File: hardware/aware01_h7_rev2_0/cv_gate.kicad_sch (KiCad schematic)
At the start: 44 parts, among them J1 CV3_IN, J10 CV2_IN, J11 V/OCT_IN, J12 CV1_IN, J13 GATE3_IN, J14 GATE4_IN, J8 GATE1_IN, J9 GATE2_IN, Q1 MMBT3904, Q2 MMBT3904, Q3 MMBT3904, Q4 MMBT3904, U11 LMV722IDR, U12 LMV722IDR

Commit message: add 5V buck converter
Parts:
- J1, J10, J11, J12, J13, J14, J8, J9: footprint Connector_Audio:Jack_3.5mm_QingPu_WQP-PJ398SM_Vertical_CircularHoles -> AudioJacks:Jack_3.5mm_QingPu_WQP-PJ398SM_Vertical
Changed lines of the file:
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@@
 			)
 		)
-		(property "Footprint" "Connector_Audio:Jack_3.5mm_QingPu_WQP-PJ398SM_Vertical_CircularHoles"
+		(property "Footprint" "AudioJacks:Jack_3.5mm_QingPu_WQP-PJ398SM_Vertical"
 			(at 27.94 96.52 0)
 			(effects
@@
 			)
 		)
-		(property "Footprint" "Connector_Audio:Jack_3.5mm_QingPu_WQP-PJ398SM_Vertical_CircularHoles"
+		(property "Footprint" "AudioJacks:Jack_3.5mm_QingPu_WQP-PJ398SM_Vertical"
 			(at 27.94 55.88 0)
 			(effects
@@
 			)
 		)
-		(property "Footprint" "Connector_Audio:Jack_3.5mm_QingPu_WQP-PJ398SM_Vertical_CircularHoles"
+		(property "Footprint" "AudioJacks:Jack_3.5mm_QingPu_WQP-PJ398SM_Vertical"
 			(at 200.66 128.27 0)
 			(effects
@@
 			)
 		)
-		(property "Footprint" "Connector_Audio:Jack_3.5mm_QingPu_WQP-PJ398SM_Vertical_CircularHoles"
+		(property "Footprint" "AudioJacks:Jack_3.5mm_QingPu_WQP-PJ398SM_Vertical"
 			(at 100.33 125.73 0)
 			(effects
@@
 			)
 		)
-		(property "Footprint" "Connector_Audio:Jack_3.5mm_QingPu_WQP-PJ398SM_Vertical_CircularHoles"
+		(property "Footprint" "AudioJacks:Jack_3.5mm_QingPu_WQP-PJ398SM_Vertical"
 			(at 200.66 57.15 0)
 			(effects
@@
 			)
 		)
-		(property "Footprint" "Connector_Audio:Jack_3.5mm_QingPu_WQP-PJ398SM_Vertical_CircularHoles"
+		(property "Footprint" "AudioJacks:Jack_3.5mm_QingPu_WQP-PJ398SM_Vertical"
 			(at 27.94 173.99 0)
 			(effects
@@
 			)
 		)
-		(property "Footprint" "Connector_Audio:Jack_3.5mm_QingPu_WQP-PJ398SM_Vertical_CircularHoles"
+		(property "Footprint" "AudioJacks:Jack_3.5mm_QingPu_WQP-PJ398SM_Vertical"
 			(at 27.94 135.89 0)
 			(effects
@@
 			)
 		)
-		(property "Footprint" "Connector_Audio:Jack_3.5mm_QingPu_WQP-PJ398SM_Vertical_CircularHoles"
+		(property "Footprint" "AudioJacks:Jack_3.5mm_QingPu_WQP-PJ398SM_Vertical"
 			(at 100.33 54.61 0)
 			(effects

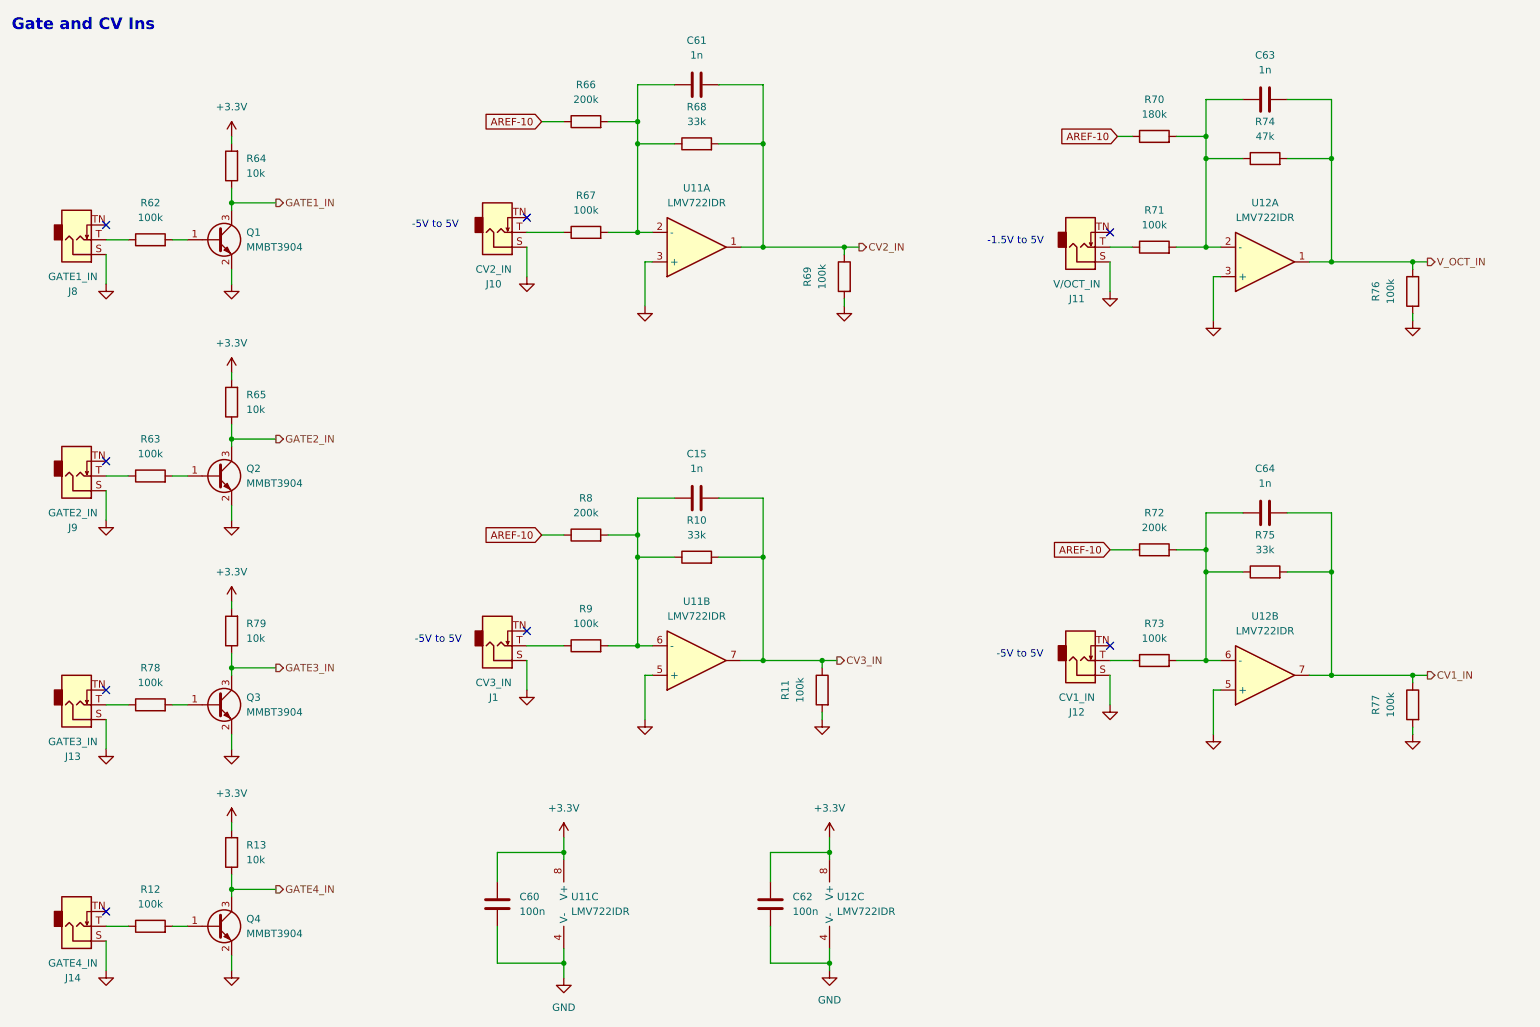
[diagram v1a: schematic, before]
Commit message: schematic formatting
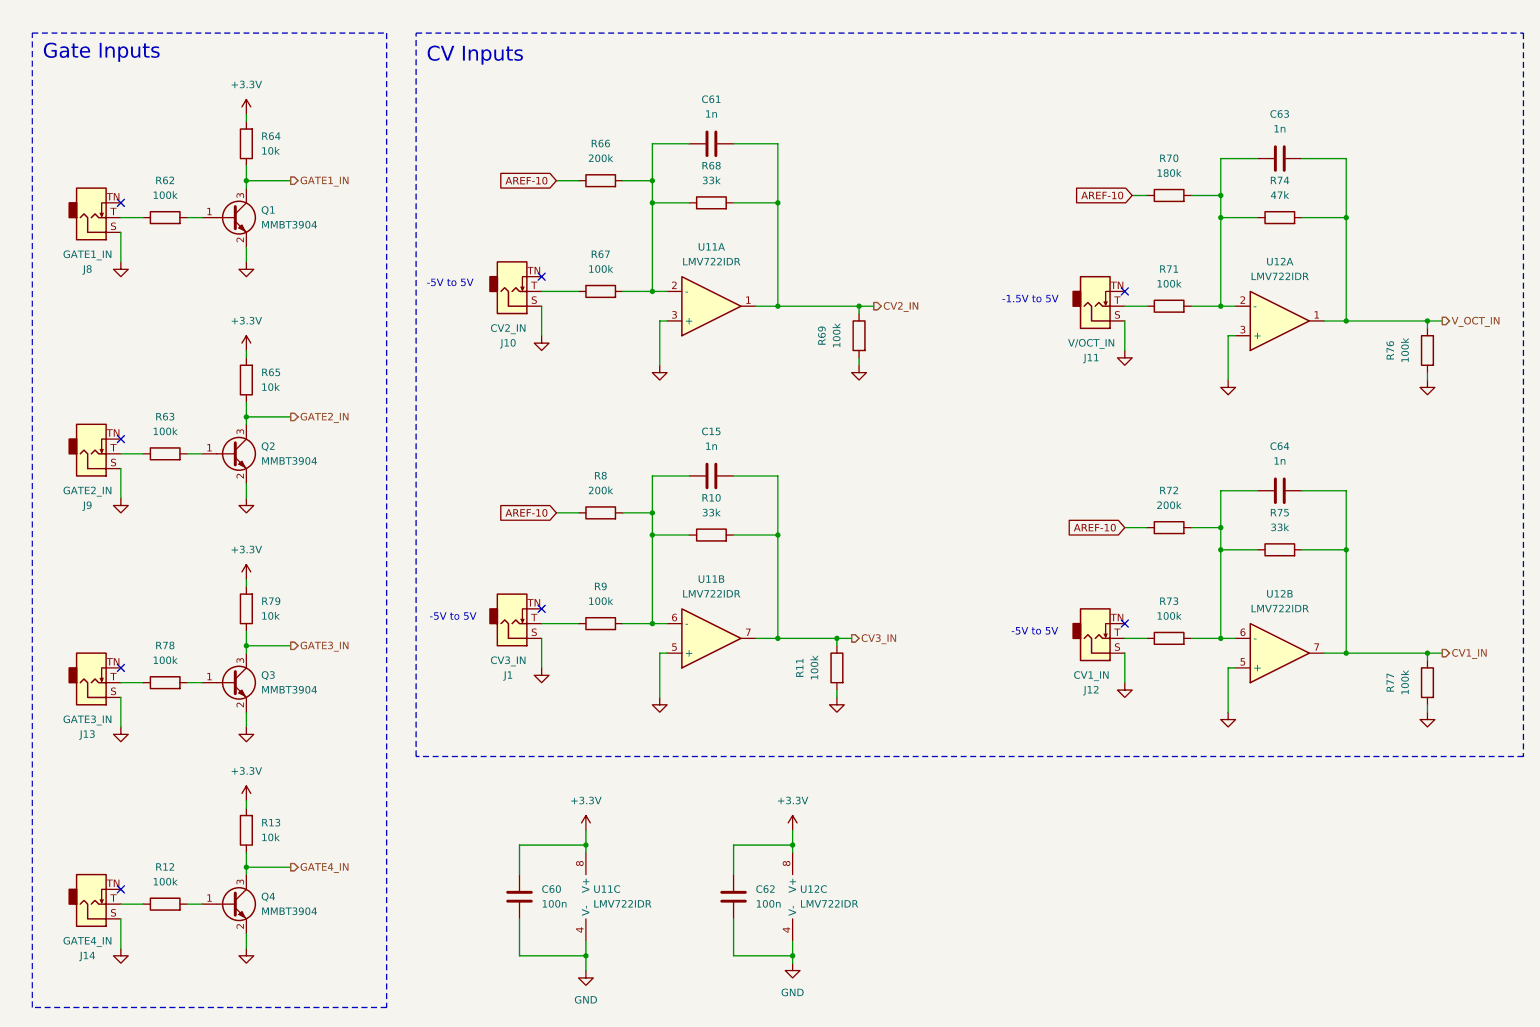
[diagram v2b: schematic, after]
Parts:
- J1, J10, J11, J12, J13, J14, J8, J9: now left out of the parts list
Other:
- note added: "CV Inputs"
- note added: "Gate Inputs"
- note removed: "Gate and CV Ins"
- moved on the sheet: C15, C60, C61, C62, C63, C64, J1, J10, J11, J12, J13, J14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

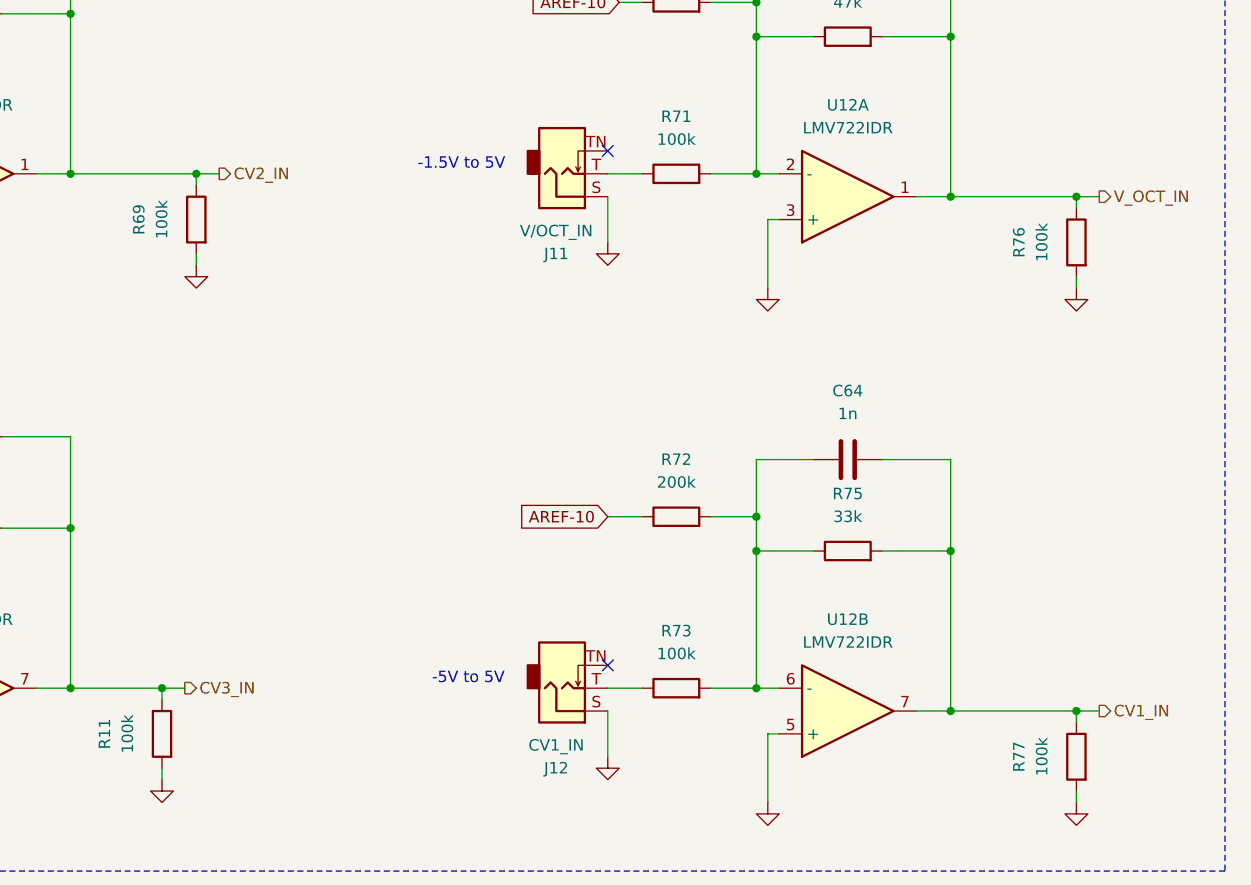
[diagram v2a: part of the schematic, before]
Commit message: refine layout, add testpoints
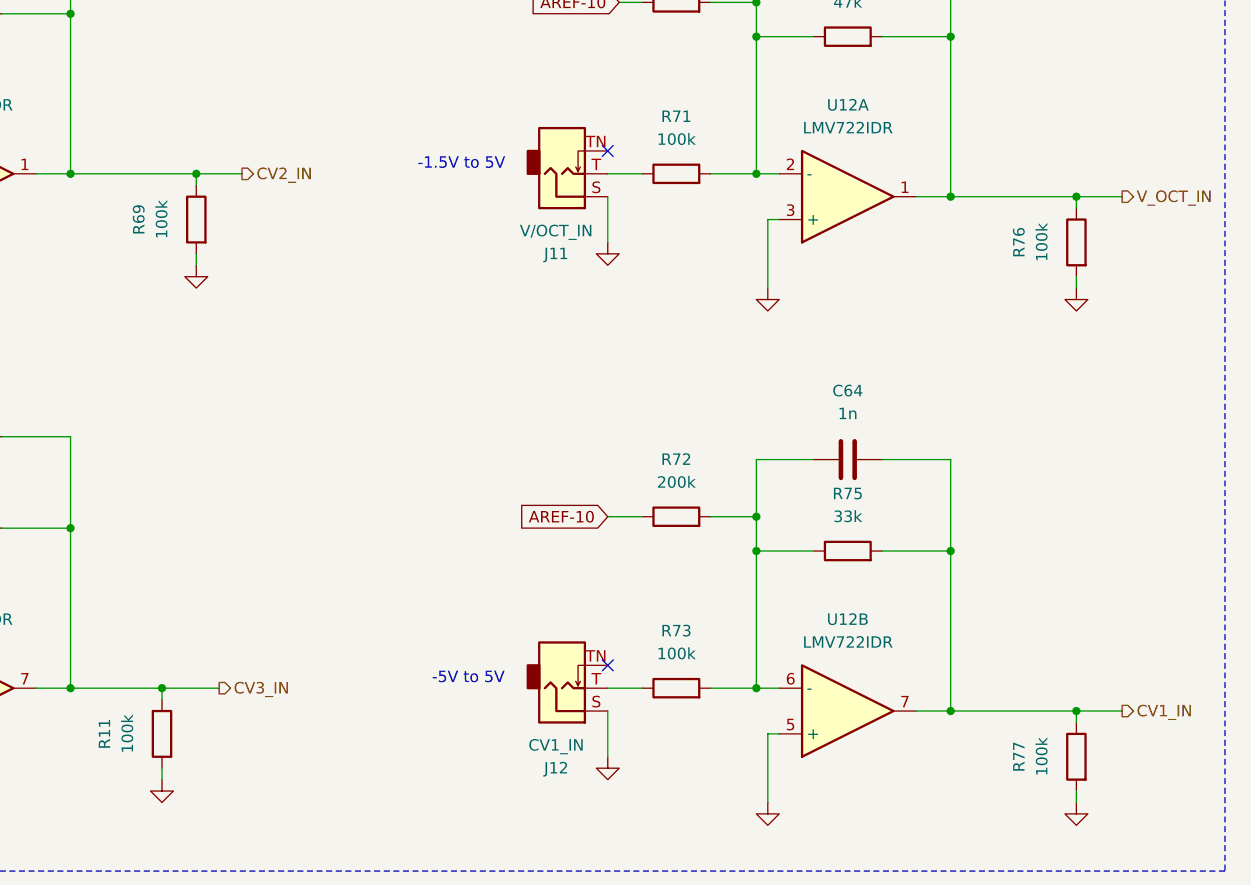
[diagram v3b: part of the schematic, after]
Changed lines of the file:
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@@
 	(wire
 		(pts
-			(xy 260.35 69.85) (xy 262.89 69.85)
+			(xy 260.35 69.85) (xy 265.43 69.85)
 		)
 		(stroke
@@
 	(wire
 		(pts
-			(xy 158.75 124.46) (xy 161.29 124.46)
-		)
-		(stroke
-			(width 0)
-			(type default)
-		)
-	)
-	(wire
-		(pts
-			(xy 162.56 67.31) (xy 165.1 67.31)
+			(xy 158.75 124.46) (xy 165.1 124.46)
+		)
+		(stroke
+			(width 0)
+			(type default)
+		)
+	)
+	(wire
+		(pts
+			(xy 162.56 67.31) (xy 167.64 67.31)
 		)
 		(stroke
@@
 	(wire
 		(pts
-			(xy 260.35 127) (xy 262.89 127)
+			(xy 260.35 127) (xy 265.43 127)
 		)
 		(stroke
@@
 	(hierarchical_label "V_OCT_IN"
 		(shape output)
-		(at 262.89 69.85 0)
+		(at 265.43 69.85 0)
 		(effects
 			(font
@@
 	(hierarchical_label "CV1_IN"
 		(shape output)
-		(at 262.89 127 0)
+		(at 265.43 127 0)
 		(effects
 			(font
@@
 	(hierarchical_label "CV3_IN"
 		(shape output)
-		(at 161.29 124.46 0)
+		(at 165.1 124.46 0)
 		(effects
 			(font
@@
 	(hierarchical_label "CV2_IN"
 		(shape output)
-		(at 165.1 67.31 0)
+		(at 167.64 67.31 0)
 		(effects
 			(font

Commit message: hw: update hw design
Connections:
- net GND: now also J13.TN, J14.TN, J8.TN, J9.TN
- no-connect marks 8 -> 4
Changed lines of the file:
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@@
+	)
+	(junction
+		(at 35.56 172.72)
+		(diameter 0)
+		(color 0 0 0 0)
 	)
 	(junction
@@
 	)
 	(junction
+		(at 35.56 54.61)
+		(diameter 0)
+		(color 0 0 0 0)
+	)
+	(junction
 		(at 57.15 86.36)
 		(diameter 0)
@@
 	)
 	(junction
+		(at 35.56 134.62)
+		(diameter 0)
+		(color 0 0 0 0)
+	)
+	(junction
 		(at 260.35 127)
 		(diameter 0)
@@
 	(junction
 		(at 246.38 127)
+		(diameter 0)
+		(color 0 0 0 0)
+	)
+	(junction
+		(at 35.56 95.25)
 		(diameter 0)
 		(color 0 0 0 0)
@@
 	)
 	(no_connect
-		(at 35.56 49.53)
-	)
-	(no_connect
-		(at 35.56 129.54)
-	)
-	(no_connect
 		(at 208.28 121.92)
-	)
-	(no_connect
-		(at 35.56 90.17)
 	)
 	(no_connect
@@
 	)
 	(no_connect
-		(at 35.56 167.64)
-	)
-	(no_connect
 		(at 208.28 64.77)
 	)
@@
 	(wire
 		(pts
+			(xy 38.1 90.17) (xy 38.1 95.25)
+		)
+		(stroke
+			(width 0)
+			(type default)
+		)
+	)
+	(wire
+		(pts
 			(xy 246.38 109.22) (xy 246.38 127)
 		)
@@
 	(wire
 		(pts
+			(xy 38.1 95.25) (xy 35.56 95.25)
+		)
+		(stroke
+			(width 0)
+			(type default)
+		)
+	)
+	(wire
+		(pts
 			(xy 148.59 106.68) (xy 148.59 124.46)
 		)
@@
 	(wire
 		(pts
+			(xy 38.1 167.64) (xy 38.1 172.72)
+		)
+		(stroke
+			(width 0)
+			(type default)
+		)
+	)
+	(wire
+		(pts
 			(xy 208.28 67.31) (xy 212.09 67.31)
 		)
@@
 	(wire
 		(pts
+			(xy 38.1 172.72) (xy 35.56 172.72)
+		)
+		(stroke
+			(width 0)
+			(type default)
+		)
+	)
+	(wire
+		(pts
 			(xy 162.56 67.31) (xy 167.64 67.31)
 		)
@@
 	(wire
 		(pts
+			(xy 38.1 54.61) (xy 35.56 54.61)
+		)
+		(stroke
+			(width 0)
+			(type default)
+		)
+	)
+	(wire
+		(pts
 			(xy 140.97 39.37) (xy 148.59 39.37)
 		)
@@
 	(wire
 		(pts
+			(xy 38.1 134.62) (xy 35.56 134.62)
+		)
+		(stroke
+			(width 0)
+			(type default)
+		)
+	)
+	(wire
+		(pts
 			(xy 224.79 99.06) (xy 224.79 105.41)
 		)
@@
 	(wire
 		(pts
+			(xy 35.56 129.54) (xy 38.1 129.54)
+		)
+		(stroke
+			(width 0)
+			(type default)
+		)
+	)
+	(wire
+		(pts
 			(xy 260.35 69.85) (xy 260.35 71.12)
 		)
@@
 	(wire
 		(pts
+			(xy 35.56 90.17) (xy 38.1 90.17)
+		)
+		(stroke
+			(width 0)
+			(type default)
+		)
+	)
+	(wire
+		(pts
 			(xy 104.14 160.02) (xy 104.14 165.1)
 		)
@@
 	(wire
 		(pts
+			(xy 35.56 49.53) (xy 38.1 49.53)
+		)
+		(stroke
+			(width 0)
+			(type default)
+		)
+	)
+	(wire
+		(pts
 			(xy 57.15 152.4) (xy 57.15 153.67)
 		)
@@
 	(wire
 		(pts
+			(xy 38.1 129.54) (xy 38.1 134.62)
+		)
+		(stroke
+			(width 0)
+			(type default)
+		)
+	)
+	(wire
+		(pts
 			(xy 260.35 137.16) (xy 260.35 135.89)
 		)
@@
 	(wire
 		(pts
+			(xy 35.56 167.64) (xy 38.1 167.64)
+		)
+		(stroke
+			(width 0)
+			(type default)
+		)
+	)
+	(wire
+		(pts
 			(xy 226.06 72.39) (xy 227.33 72.39)
 		)
@@
 		)
 		(stroke
+			(width 0)
+			(type default)
+		)
+	)
+	(wire
+		(pts
+			(xy 38.1 49.53) (xy 38.1 54.61)
+		)
+		(stroke
